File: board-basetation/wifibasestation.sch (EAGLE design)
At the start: 25 parts, among them J1 SWD_SHROUD_SMD, Q1 MOSFET-PCHANNELSMD

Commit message: some routing
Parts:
- removed C7: (no value), rcl:C-EUC0603K
- removed Q1: MOSFET-PCHANNELSMD, SparkFun-DiscreteSemi:MOSFET-PCHANNELSMD
- added C10, C11, C8, C9: (no value), rcl:C-EUC0603K
- added IC1: 1117EMP, dtb:1117EMP
- added IC2: HTU21D, Mine:HTU21D
- added R5: (no value), rcl:R-EU_R0603
- added S1: SWITCH-MOMENTARY-2SMD, Mine:SWITCH-MOMENTARY-2SMD
- added U$4: BUS-SMA, Ava:BUS-SMA
- LED1, LED2, LED3: device dtb:LEDSMT1206 -> led:LEDCHIP-LED0805
- U$3: value CRYSTAL-GROUNDED -> LMT85; device SparkFun-FreqCtrl:CRYSTAL-GROUNDED -> Mine:LMT85
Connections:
- removed net N$1: SV1.1
- removed net N$6: SV1.7
- new net CH_PD: SV1.6, U$1.PF0
- new net DIO0: U$1.PB8, U$2.DIO0
- new net I2C2_SCL: IC2.SCK, R1.1, U$1.PB10
- new net I2C2_SDA: IC2.DATA, R5.1, U$1.PB11
- new net MISO: U$1.PB4, U$2.MISO
- new net MOSI: U$1.PB5, U$2.MOSI
- new net N$19: U$2.ANT, U$4.1
- new net N$20: LED3.A, RN1D.2
- new net N$21: RN1C.1, U$1.PC14
- new net N$22: RN1B.1, U$1.PC15
- new net N$23: U$1.PA8
- new net N$24: U$1.PA9
- new net N$26: U$1.PB13
- new net N$27: U$1.PB14
- new net NSS: U$1.PB9, U$2.NSS
- new net RST: U$2.RESET
- new net SCK: U$1.PB3, U$2.SCK
- new net USART1_RX: SV1.8, U$1.PB7
- new net USART1_TX: SV1.1, U$1.PB6
- new net USART2_RX: JP3.3, U$1.PA3
- new net USART2_TX: JP3.2, U$1.PA2
- new net W_RST: SV1.4, U$1.PF1
- net +3V3: now also C10.1, C11.1, C6.1, C9.1, IC1.VO, IC2.VDD, JP3.4, R1.2, R5.2, S1.2, SV1.2, U$2.VCC
- net GND: now also C10.2, C11.2, C8.2, C9.2, IC1.ADJ, IC2.GND, JP3.6, LED1.C, LED2.C, LED3.C, SV1.7, U$2.GNDA, U$2.GNDB, U$4.GND; no longer C7.2, U$3.3
- net N$10: now also LED2.A, RN1C.2; no longer Q1.S
- net N$12: now also U$1.PA5; no longer C7.1, R1.2, U$3.1
- net N$14: now also U$1.PA6; no longer R1.1, U$1.PF1
- net N$15: now also S1.1
- net N$16: now also U$1.PA7; no longer C6.1, U$1.PF0, U$3.2
- net N$2: now also RN1D.1, U$1.PC13; no longer Q1.D, SV1.2
- net N$3: now also U$1.PA0; no longer SV1.4
- net N$7: now also U$1.PA1; no longer SV1.6
- net N$8: now also U$1.PA4; no longer SV1.8
- net N$9: now also LED1.A, RN1A.2, RN1B.2; no longer Q1.G
- net VBUS: now also C8.1, IC1.VI
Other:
- note added: "spec"
- moved on the sheet: C6, R1, RN1A, RN1B, RN1C, RN1D

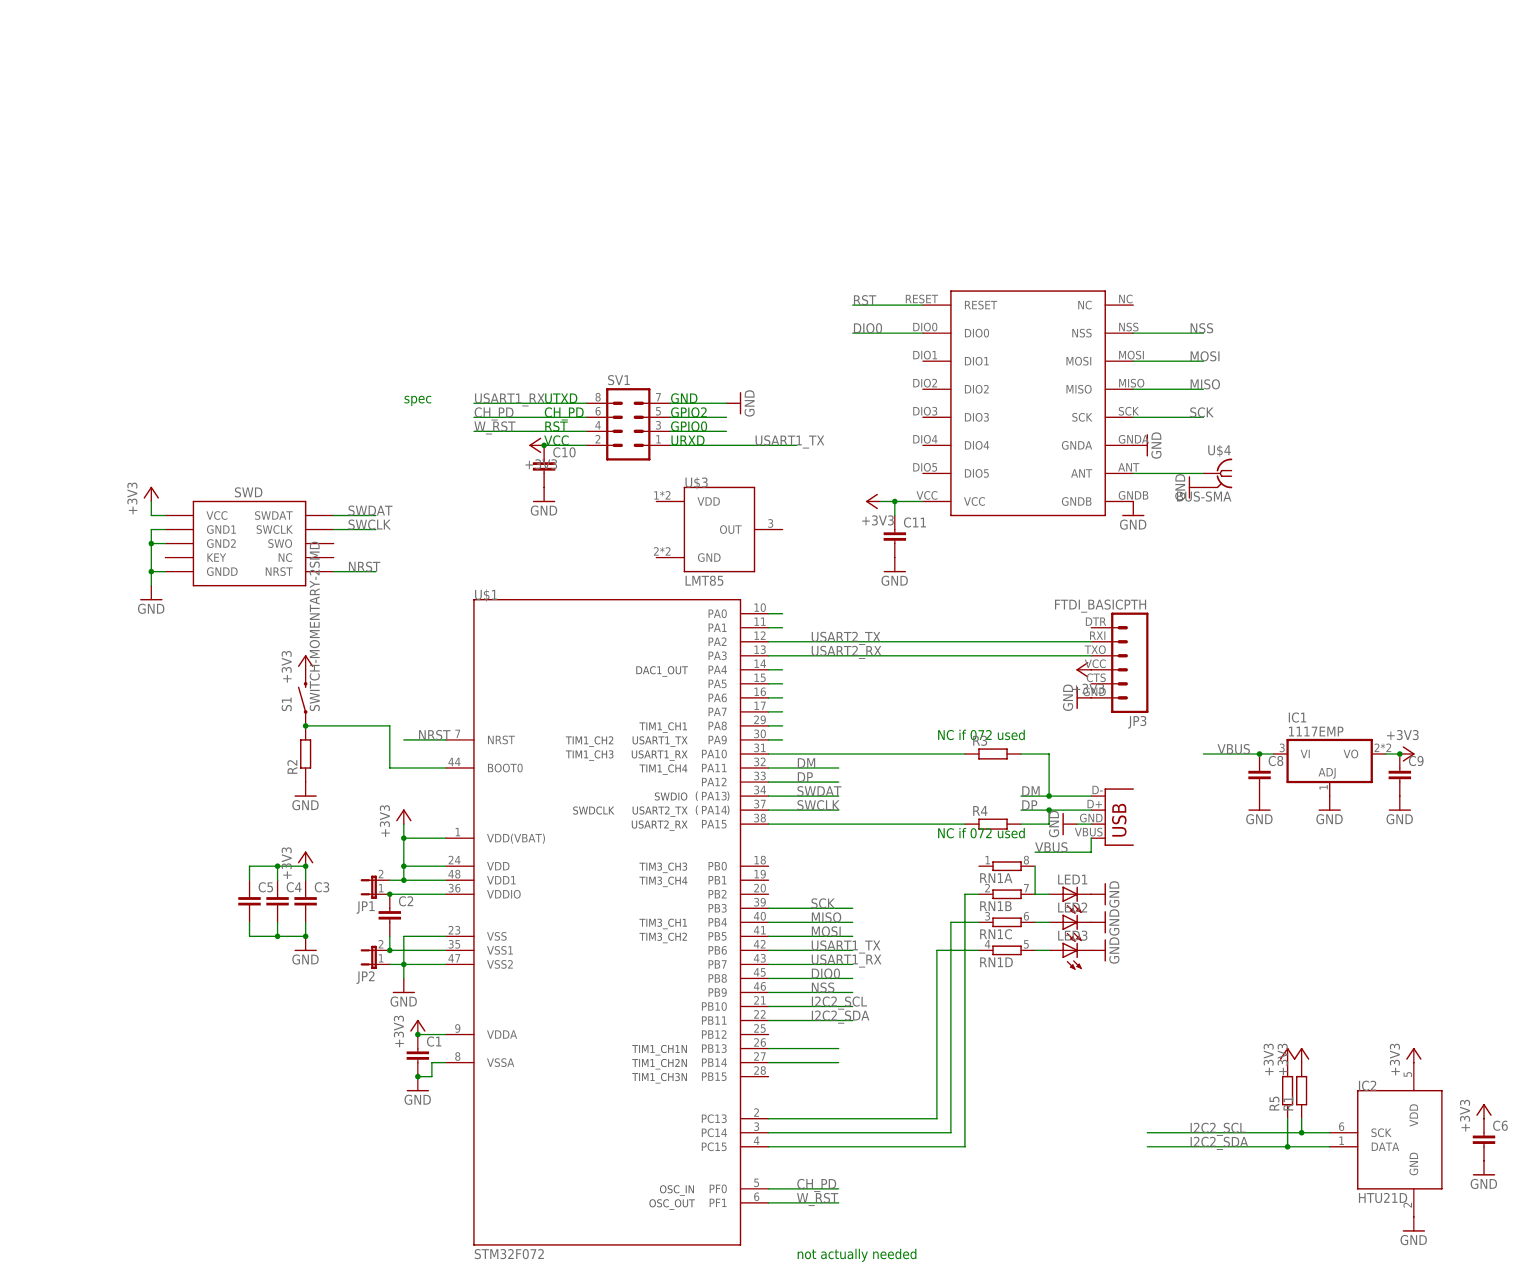
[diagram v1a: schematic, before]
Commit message: moved to smd esp
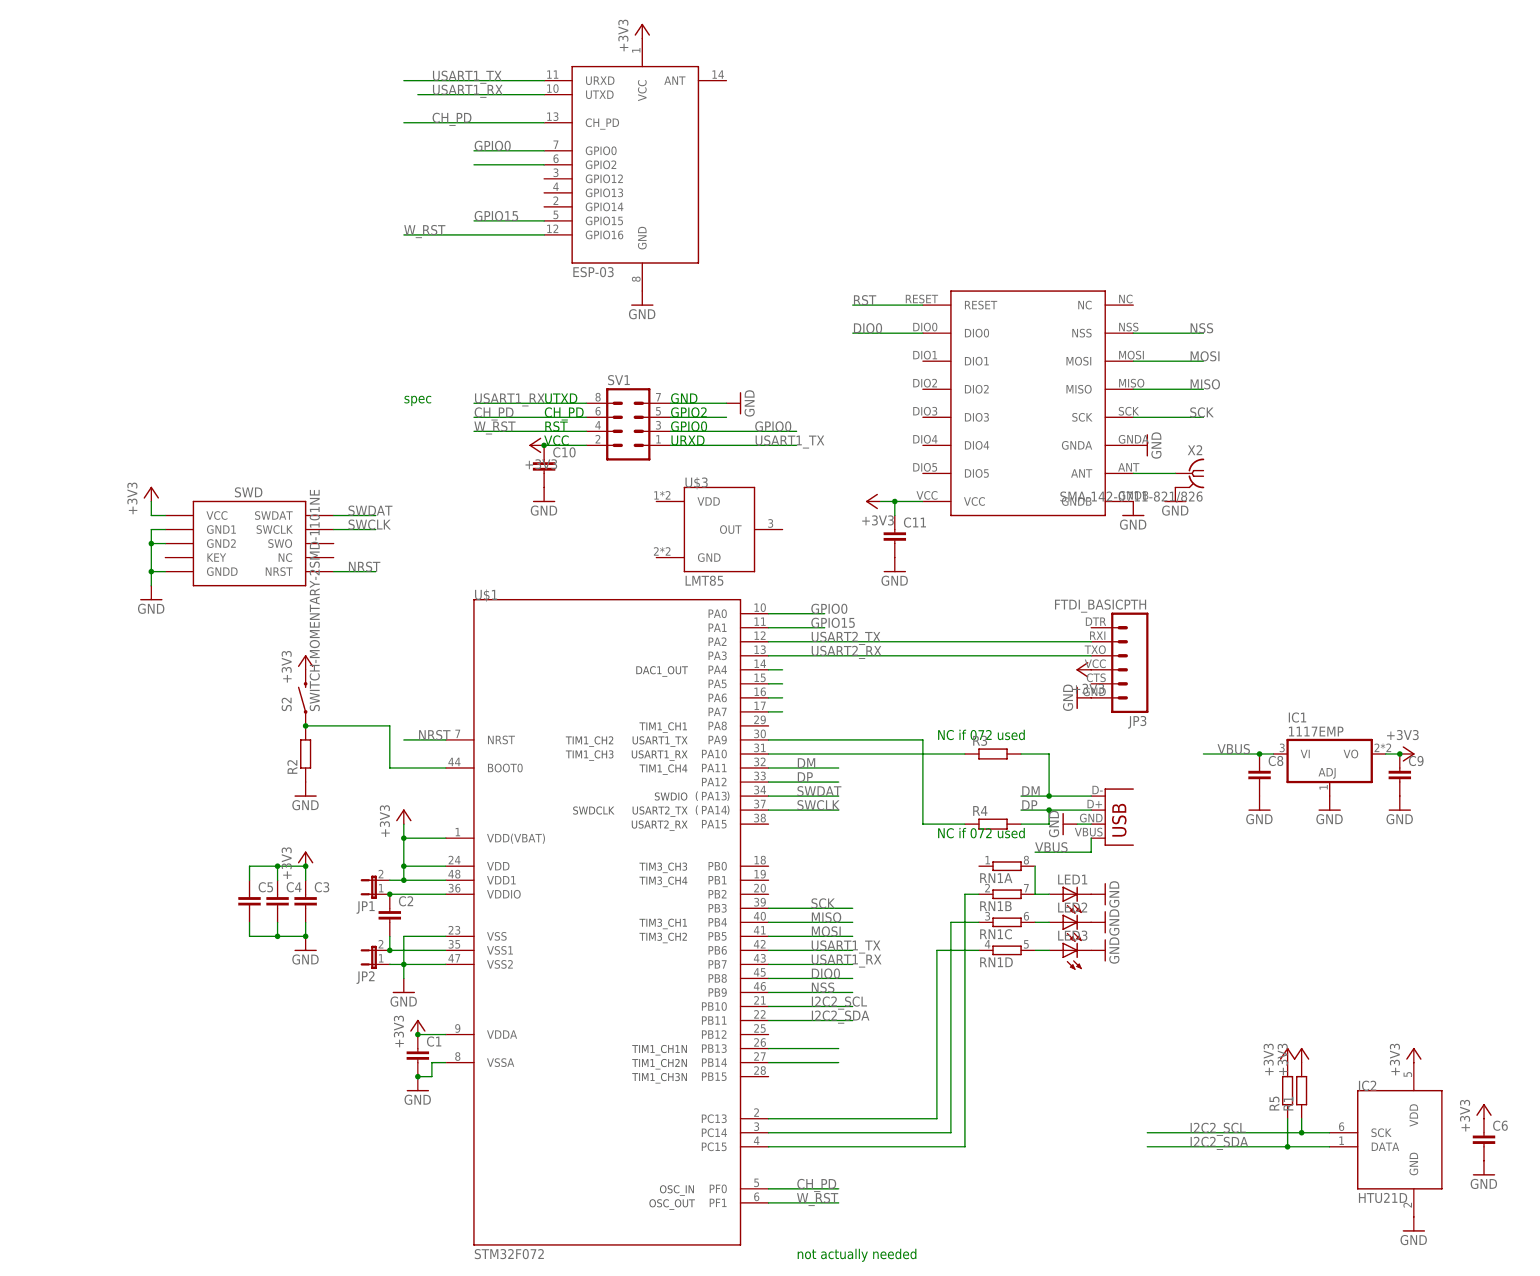
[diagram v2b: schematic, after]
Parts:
- removed S1: SWITCH-MOMENTARY-2SMD, Mine:SWITCH-MOMENTARY-2SMD
- removed U$4: BUS-SMA, Ava:BUS-SMA
- added S2: SWITCH-MOMENTARY-2SMD-1101NE, SparkFun-Electromechanical:SWITCH-MOMENTARY-2SMD-1101NE
- added X1: ESP-03, Mine:ESP-03
- added X2: SMA-142-0711-821/826, con-coax:SMA-142-0711-821/826
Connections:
- removed net N$19: U$2.ANT, U$4.1
- removed net N$23: U$1.PA8
- removed net N$24: U$1.PA9
- removed net N$3: U$1.PA0
- removed net N$4: SV1.3
- removed net N$7: U$1.PA1
- new net GPIO0: SV1.3, U$1.PA0, X1.GPIO0
- new net GPIO15: U$1.PA1, X1.GPIO15
- new net N$1: X1.GPIO2
- new net N$6: U$2.ANT, X2.1
- net +3V3: now also S2.2, X1.VCC; no longer S1.2
- net CH_PD: now also X1.CH_PD
- net GND: now also X1.GND, X2.2; no longer U$4.GND
- net N$15: now also S2.1; no longer S1.1
- net N$18: now also U$1.PA9; no longer U$1.PA15
- net USART1_RX: now also X1.UTXD
- net USART1_TX: now also X1.URXD
- net W_RST: now also X1.GPIO16
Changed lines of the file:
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@@
 <part name="R4" library="rcl" deviceset="R-EU_" device="R0603"/>
 <part name="GND9" library="supply1" deviceset="GND" device=""/>
-<part name="U$4" library="Ava" deviceset="BUS-SMA" device=""/>
 <part name="+3V5" library="supply1" deviceset="+3V3" device=""/>
 <part name="C8" library="rcl" deviceset="C-EU" device="C0603K"/>
@@
 <part name="GND10" library="supply1" deviceset="GND" device=""/>
 <part name="GND13" library="supply1" deviceset="GND" device=""/>
-<part name="GND14" library="supply1" deviceset="GND" device=""/>
 <part name="GND16" library="supply1" deviceset="GND" device=""/>
 <part name="GND17" library="supply1" deviceset="GND" device=""/>
@@
 <part name="GND4" library="supply1" deviceset="GND" device=""/>
 <part name="+3V8" library="supply1" deviceset="+3V3" device=""/>
-<part name="S1" library="Mine" deviceset="SWITCH-MOMENTARY-2" device="SMD"/>
 <part name="+3V9" library="supply1" deviceset="+3V3" device=""/>
 <part name="U$3" library="Mine" deviceset="LMT85" device=""/>
@@
 <part name="GND6" library="supply1" deviceset="GND" device=""/>
 <part name="GND21" library="supply1" deviceset="GND" device=""/>
+<part name="X1" library="Mine" deviceset="ESP-03" device=""/>
+<part name="X2" library="con-coax" deviceset="SMA-" device="142-0711-821/826"/>
+<part name="S2" library="SparkFun-Electromechanical" deviceset="SWITCH-MOMENTARY-2" device="SMD-1101NE"/>
+<part name="GND14" library="supply1" deviceset="GND" device=""/>
+<part name="GND22" library="supply1" deviceset="GND" device=""/>
+<part name="+3V14" library="supply1" deviceset="+3V3" device=""/>
 </parts>
 <sheets>
@@
 <instance part="R4" gate="G$1" x="165.1" y="91.44"/>
 <instance part="GND9" gate="1" x="177.8" y="91.44" rot="R270"/>
-<instance part="U$4" gate="G$1" x="205.74" y="154.94" rot="MR0"/>
 <instance part="+3V5" gate="G$1" x="241.3" y="104.14" rot="R270"/>
 <instance part="C8" gate="G$1" x="213.36" y="101.6"/>
@@
 <instance part="GND10" gate="1" x="226.06" y="93.98"/>
 <instance part="GND13" gate="1" x="190.5" y="147.32"/>
-<instance part="GND14" gate="1" x="200.66" y="152.4" rot="R270"/>
 <instance part="GND16" gate="1" x="193.04" y="160.02" rot="R90"/>
 <instance part="GND17" gate="1" x="185.42" y="68.58" rot="R90"/>
@@
 <instance part="GND4" gate="1" x="180.34" y="114.3" rot="R270"/>
 <instance part="+3V8" gate="G$1" x="180.34" y="119.38" rot="R90"/>
-<instance part="S1" gate="G$1" x="40.64" y="114.3" rot="R90"/>
 <instance part="+3V9" gate="G$1" x="40.64" y="121.92"/>
 <instance part="U$3" gate="G$1" x="119.38" y="144.78"/>
@@
 <instance part="GND6" gate="1" x="254" y="27.94"/>
 <instance part="GND21" gate="1" x="119.38" y="167.64" rot="R90"/>
+<instance part="X1" gate="G$1" x="96.52" y="220.98"/>
+<instance part="X2" gate="G1" x="200.66" y="154.94" rot="MR0"/>
+<instance part="S2" gate="G$1" x="40.64" y="114.3" rot="R90"/>
+<instance part="GND14" gate="1" x="198.12" y="149.86"/>
+<instance part="GND22" gate="1" x="101.6" y="185.42"/>
+<instance part="+3V14" gate="G$1" x="101.6" y="236.22"/>
 </instances>
 <busses>
@@
 <label x="129.54" y="22.86" size="1.778" layer="95"/>
 </segment>
-</net>
-<net name="N$4" class="0">
-<segment>
-<pinref part="SV1" gate="G$1" pin="3"/>
-<wire x1="106.68" y1="162.56" x2="116.84" y2="162.56" width="0.1524" layer="91"/>
+<segment>
+<wire x1="83.82" y1="198.12" x2="58.42" y2="198.12" width="0.1524" layer="91"/>
+<label x="58.42" y="198.12" size="1.778" layer="95"/>
+<pinref part="X1" gate="G$1" pin="GPIO16"/>
 </segment>
 </net>
@@
 <wire x1="137.16" y1="25.4" x2="124.46" y2="25.4" width="0.1524" layer="91"/>
 <label x="129.54" y="25.4" size="1.778" layer="95"/>
+</segment>
+<segment>
+<wire x1="83.82" y1="218.44" x2="58.42" y2="218.44" width="0.1524" layer="91"/>
+<pinref part="X1" gate="G$1" pin="CH_PD"/>
+<label x="63.5" y="218.44" size="1.778" layer="95"/>
 </segment>
 </net>
@@
 </segment>
 <segment>
-<pinref part="U$4" gate="G$1" pin="GND"/>
-<pinref part="GND14" gate="1" pin="GND"/>
-</segment>
-<segment>
 <pinref part="U$2" gate="A" pin="GNDA"/>
 <pinref part="GND16" gate="1" pin="GND"/>
@@
 <wire x1="106.68" y1="167.64" x2="116.84" y2="167.64" width="0.1524" layer="91"/>
 <pinref part="GND21" gate="1" pin="GND"/>
+</segment>
+<segment>
+<pinref part="X2" gate="G1" pin="2"/>
+<pinref part="GND14" gate="1" pin="GND"/>
+</segment>
+<segment>
+<pinref part="X1" gate="G$1" pin="GND"/>
+<pinref part="GND22" gate="1" pin="GND"/>
 </segment>
 </net>
@@
 </segment>
 <segment>
-<pinref part="S1" gate="G$1" pin="2"/>
 <pinref part="+3V9" gate="G$1" pin="+3V3"/>
+<pinref part="S2" gate="G$1" pin="2"/>
 </segment>
 <segment>
@@
 <pinref part="C6" gate="G$1" pin="1"/>
 <pinref part="+3V13" gate="G$1" pin="+3V3"/>
+</segment>
+<segment>
+<pinref part="X1" gate="G$1" pin="VCC"/>
+<pinref part="+3V14" gate="G$1" pin="+3V3"/>
 </segment>
 </net>
@@
 <pinref part="R2" gate="G$1" pin="2"/>
 <junction x="40.64" y="109.22"/>
-<pinref part="S1" gate="G$1" pin="1"/>
+<pinref part="S2" gate="G$1" pin="1"/>
 </segment>
 </net>
@@
 <net name="N$18" class="0">
 <segment>
-<pinref part="U$1" gate="G$1" pin="PA15"/>
 <pinref part="R4" gate="G$1" pin="1"/>
-<wire x1="124.46" y1="91.44" x2="160.02" y2="91.44" width="0.1524" layer="91"/>
+<pinref part="U$1" gate="G$1" pin="PA9"/>
+<wire x1="152.4" y1="91.44" x2="160.02" y2="91.44" width="0.1524" layer="91"/>
+<wire x1="124.46" y1="106.68" x2="152.4" y2="106.68" width="0.1524" layer="91"/>
+<wire x1="152.4" y1="106.68" x2="152.4" y2="91.44" width="0.1524" layer="91"/>
 </segment>
 </net>
@@
 </segment>
 </net>
-<net name="N$19" class="0">
-<segment>
-<pinref part="U$2" gate="A" pin="ANT"/>
-<pinref part="U$4" gate="G$1" pin="1"/>
-<wire x1="203.2" y1="154.94" x2="190.5" y2="154.94" width="0.1524" layer="91"/>
-</segment>
-</net>
 <net name="N$9" class="0">
 <segment>
@@
 <label x="71.12" y="167.64" size="1.778" layer="95"/>
 </segment>
+<segment>
+<wire x1="83.82" y1="223.52" x2="60.96" y2="223.52" width="0.1524" layer="91"/>
+<pinref part="X1" gate="G$1" pin="UTXD"/>
+<label x="63.5" y="223.52" size="1.778" layer="95"/>
+</segment>
 </net>
 <net name="USART1_TX" class="0">
@@
 <label x="121.92" y="160.02" size="1.778" layer="95"/>
 </segment>
-</net>
-<net name="N$3" class="0">
-<segment>
-<pinref part="U$1" gate="G$1" pin="PA0"/>
-<wire x1="124.46" y1="129.54" x2="127" y2="129.54" width="0.1524" layer="91"/>
-</segment>
-</net>
-<net name="N$7" class="0">
-<segment>
-<pinref part="U$1" gate="G$1" pin="PA1"/>
-<wire x1="127" y1="127" x2="124.46" y2="127" width="0.1524" layer="91"/>
+<segment>
+<wire x1="58.42" y1="226.06" x2="83.82" y2="226.06" width="0.1524" layer="91"/>
+<pinref part="X1" gate="G$1" pin="URXD"/>
+<label x="63.5" y="226.06" size="1.778" layer="95"/>
 </segment>
 </net>
@@
 <pinref part="U$1" gate="G$1" pin="PA7"/>
 <wire x1="127" y1="111.76" x2="124.46" y2="111.76" width="0.1524" layer="91"/>
-</segment>
-</net>
-<net name="N$23" class="0">
-<segment>
-<pinref part="U$1" gate="G$1" pin="PA8"/>
-<wire x1="124.46" y1="109.22" x2="127" y2="109.22" width="0.1524" layer="91"/>
-</segment>
-</net>
-<net name="N$24" class="0">
-<segment>
-<pinref part="U$1" gate="G$1" pin="PA9"/>
-<wire x1="127" y1="106.68" x2="124.46" y2="106.68" width="0.1524" layer="91"/>
 </segment>
 </net>
@@
 </segment>
 </net>
+<net name="N$6" class="0">
+<segment>
+<pinref part="U$2" gate="A" pin="ANT"/>
+<pinref part="X2" gate="G1" pin="1"/>
+<wire x1="198.12" y1="154.94" x2="190.5" y2="154.94" width="0.1524" layer="91"/>
+</segment>
+</net>
+<net name="GPIO15" class="0">
+<segment>
+<pinref part="X1" gate="G$1" pin="GPIO15"/>
+<wire x1="83.82" y1="200.66" x2="71.12" y2="200.66" width="0.1524" layer="91"/>
+<label x="71.12" y="200.66" size="1.778" layer="95"/>
+</segment>
+<segment>
+<pinref part="U$1" gate="G$1" pin="PA1"/>
+<label x="132.08" y="127" size="1.778" layer="95"/>
+<wire x1="134.62" y1="127" x2="124.46" y2="127" width="0.1524" layer="91"/>
+</segment>
+</net>
+<net name="GPIO0" class="0">
+<segment>
+<pinref part="X1" gate="G$1" pin="GPIO0"/>
+<wire x1="83.82" y1="213.36" x2="71.12" y2="213.36" width="0.1524" layer="91"/>
+<label x="71.12" y="213.36" size="1.778" layer="95"/>
+</segment>
+<segment>
+<pinref part="SV1" gate="G$1" pin="3"/>
+<wire x1="106.68" y1="162.56" x2="129.54" y2="162.56" width="0.1524" layer="91"/>
+<label x="121.92" y="162.56" size="1.778" layer="95"/>
+</segment>
+<segment>
+<pinref part="U$1" gate="G$1" pin="PA0"/>
+<label x="132.08" y="129.54" size="1.778" layer="95"/>
+<wire x1="124.46" y1="129.54" x2="134.62" y2="129.54" width="0.1524" layer="91"/>
+</segment>
+</net>
+<net name="N$1" class="0">
+<segment>
+<pinref part="X1" gate="G$1" pin="GPIO2"/>
+<wire x1="83.82" y1="210.82" x2="71.12" y2="210.82" width="0.1524" layer="91"/>
+</segment>
+</net>

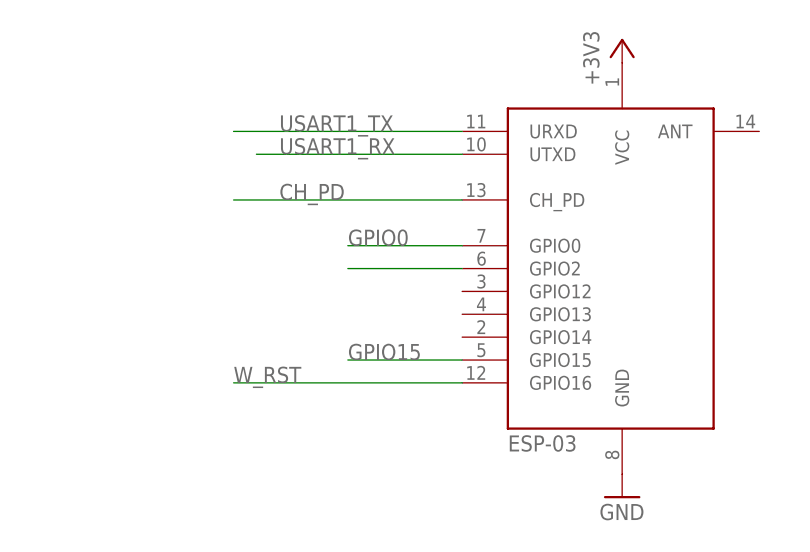
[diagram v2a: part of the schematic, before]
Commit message: routing improved
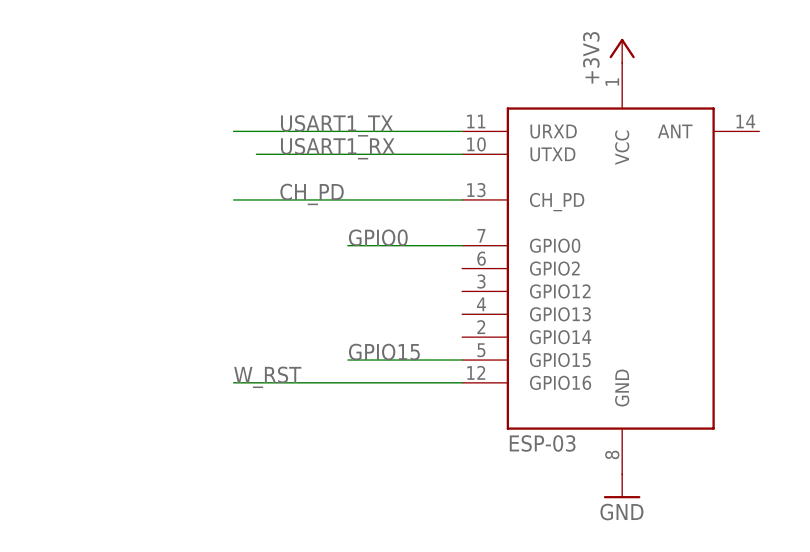
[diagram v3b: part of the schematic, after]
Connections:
- removed net N$1: X1.GPIO2
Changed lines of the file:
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@@
-</segment>
-</net>
-<net name="N$1" class="0">
-<segment>
-<pinref part="X1" gate="G$1" pin="GPIO2"/>
-<wire x1="83.82" y1="210.82" x2="71.12" y2="210.82" width="0.1524" layer="91"/>
 </segment>
 </net>
